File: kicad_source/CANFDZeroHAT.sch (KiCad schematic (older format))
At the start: 24 parts, among them CN1 RASPI-IO, CN2 691322310004, CN3 GH_SM04B-GHS-TB, CN4 GH_SM04B-GHS-TB, SW1 JS202011JCQN, U1 MCP2518FD, U2 TCAN332GDR, Y1 RH100-20.000-20-3030-TR

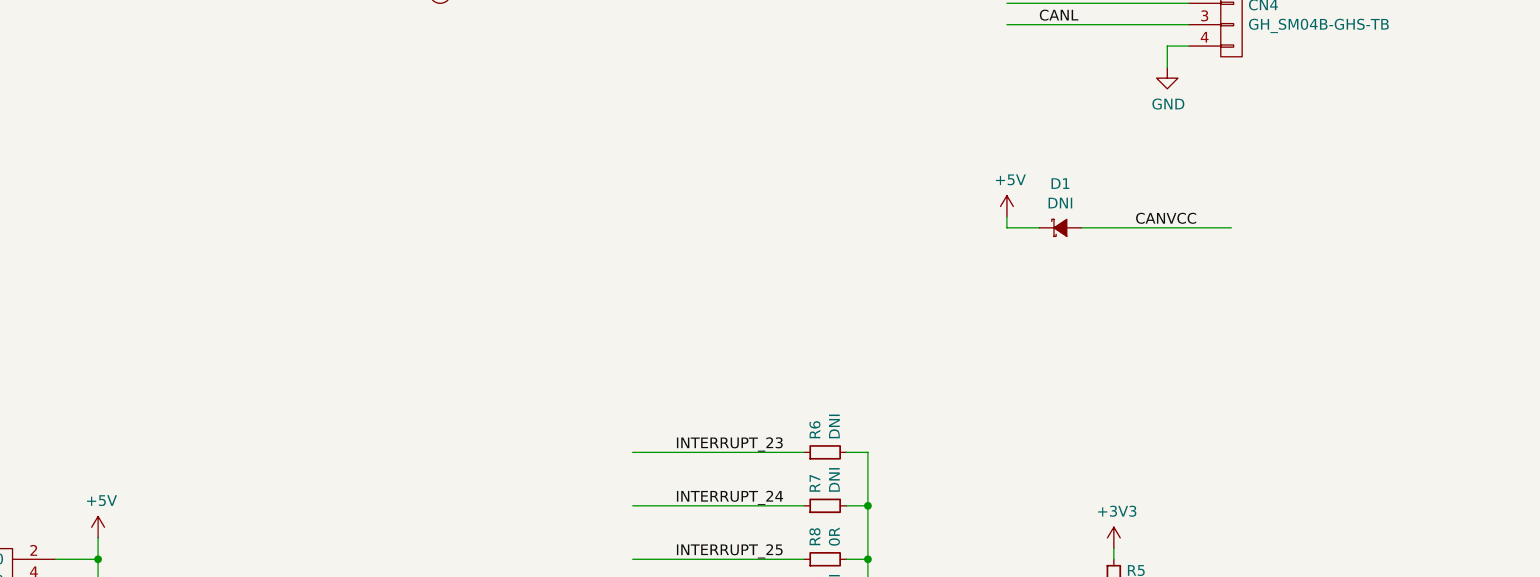
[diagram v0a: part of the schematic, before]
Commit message: updated schematic, added fuse and debug leds
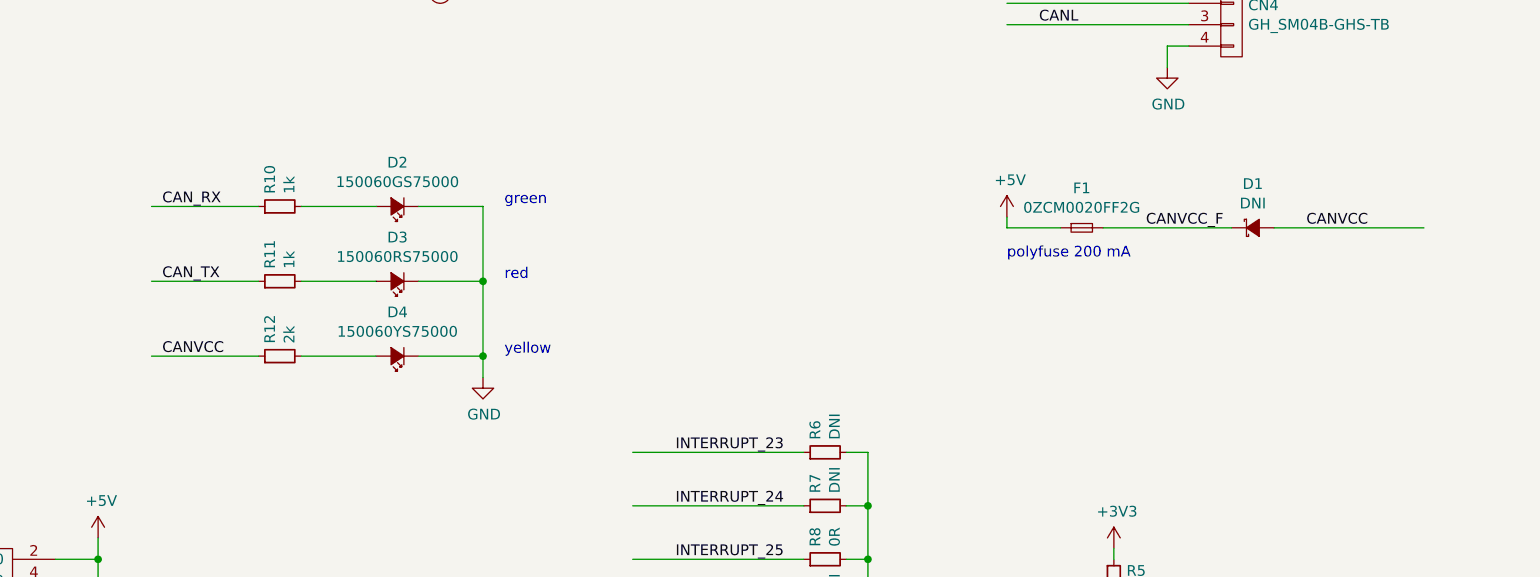
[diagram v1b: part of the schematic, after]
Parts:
- added D2: 150060GS75000, symbol devices:Led_Small
- added D3: 150060RS75000, symbol devices:Led_Small
- added D4: 150060YS75000, symbol devices:Led_Small
- added F1: 0ZCM0020FF2G, resistors:R_0603, symbol devices:F_Small
- added R10, R11: 1k, resistors:R_0603, symbol devices:R_0603
- added R12: 2k, resistors:R_0603, symbol devices:R_0603
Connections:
- net labels added: CANVCC_F
- wire segments 122 -> 135
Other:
- note added: "green"
- note added: "polyfuse 200 mA"
- note added: "red"
- note added: "yellow"
- moved on the sheet: D1
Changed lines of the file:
@@
 Sheet 1 1
 Title "CANFDZeroHAT"
-Date "2020-12-20"
-Rev "0.1"
+Date "2021-01-02"
+Rev "0.2"
 Comp "generationmake"
 Comment1 ""
@@
 L devices:D_Schottky_Small D?
 U 1 1 5FD7527E
-P 9300 3400
+P 10200 3400
 AR Path="/5FD58A5B/5FD7527E" Ref="D?"  Part="1"
 AR Path="/5FD7527E" Ref="D1"  Part="1"
-F 0 "D1" H 9300 3605 50  0000 C CNN
-F 1 "DNI" H 9300 3514 50  0000 C CNN
-F 2 "diodes:SOD-123" V 9300 3400 50  0001 C CNN
-F 3 "" V 9300 3400 50  0000 C CNN
-	1    9300 3400
+F 0 "D1" H 10200 3605 50  0000 C CNN
+F 1 "DNI" H 10200 3514 50  0000 C CNN
+F 2 "diodes:SOD-123" V 10200 3400 50  0001 C CNN
+F 3 "" V 10200 3400 50  0000 C CNN
+	1    10200 3400
 	1    0    0    -1
 $EndComp
@@
 $EndComp
 Wire Wire Line
-	10100 3400 9400 3400
-Wire Wire Line
-	9200 3400 9050 3400
-Wire Wire Line
 	9050 3400 9050 3350
 Text Label 9200 2250 0    50   ~ 0
@@
 Text Label 9200 1300 0    50   ~ 0
 CANVCC
-Text Label 9650 3400 0    50   ~ 0
-CANVCC
+Text Label 9700 3400 0    50   ~ 0
+CANVCC_F
 Wire Wire Line
 	9050 2250 9900 2250
@@
 Wire Wire Line
 	3000 2100 3000 2300
+$Comp
+L devices:F_Small F1
+U 1 1 5FF07EC2
+P 9400 3400
+F 0 "F1" H 9400 3585 50  0000 C CNN
+F 1 "0ZCM0020FF2G" H 9400 3494 50  0000 C CNN
+F 2 "resistors:R_0603" H 9400 3400 50  0001 C CNN
+F 3 "" H 9400 3400 50  0000 C CNN
+	1    9400 3400
+	1    0    0    -1
+$EndComp
+Text Label 10450 3400 0    50   ~ 0
+CANVCC
+Text Notes 9050 3550 0    50   ~ 0
+polyfuse 200 mA
+Wire Wire Line
+	9050 3400 9300 3400
+Wire Wire Line
+	9500 3400 10100 3400
+Wire Wire Line
+	11000 3400 10300 3400
+$Comp
+L devices:Led_Small D2
+U 1 1 5FF1A54D
+P 6200 3300
+F 0 "D2" H 6200 3095 50  0000 C CNN
+F 1 "150060GS75000" H 6200 3186 50  0000 C CNN
+F 2 "" V 6200 3300 50  0000 C CNN
+F 3 "" V 6200 3300 50  0000 C CNN
+	1    6200 3300
+	-1   0    0    1
+$EndComp
+$Comp
+L devices:R_0603 R?
+U 1 1 5FF1C600
+P 5650 3300
+AR Path="/5FD58A5B/5FF1C600" Ref="R?"  Part="1"
+AR Path="/5FF1C600" Ref="R10"  Part="1"
+F 0 "R10" H 5709 3346 50  0000 L CNN
+F 1 "1k" H 5709 3255 50  0000 L CNN
+F 2 "resistors:R_0603" H 5650 3150 50  0001 C CNN
+F 3 "" H 5650 3300 50  0000 C CNN
+	1    5650 3300
+	0    -1   -1   0
+$EndComp
+Text Notes 6700 3300 0    50   ~ 0
+green
+$Comp
+L devices:Led_Small D3
+U 1 1 5FF1E649
+P 6200 3650
+F 0 "D3" H 6200 3445 50  0000 C CNN
+F 1 "150060RS75000" H 6200 3536 50  0000 C CNN
+F 2 "" V 6200 3650 50  0000 C CNN
+F 3 "" V 6200 3650 50  0000 C CNN
+	1    6200 3650
+	-1   0    0    1
+$EndComp
+$Comp
+L devices:R_0603 R?
+U 1 1 5FF1E7A3
+P 5650 3650
+AR Path="/5FD58A5B/5FF1E7A3" Ref="R?"  Part="1"
+AR Path="/5FF1E7A3" Ref="R11"  Part="1"
+F 0 "R11" H 5709 3696 50  0000 L CNN
+F 1 "1k" H 5709 3605 50  0000 L CNN
+F 2 "resistors:R_0603" H 5650 3500 50  0001 C CNN
+F 3 "" H 5650 3650 50  0000 C CNN
+	1    5650 3650
+	0    -1   -1   0
+$EndComp
+Text Notes 6700 3650 0    50   ~ 0
+red
+$Comp
+L devices:Led_Small D4
+U 1 1 5FF239FB
+P 6200 4000
+F 0 "D4" H 6200 3795 50  0000 C CNN
+F 1 "150060YS75000" H 6200 3886 50  0000 C CNN
+F 2 "" V 6200 4000 50  0000 C CNN
+F 3 "" V 6200 4000 50  0000 C CNN
+	1    6200 4000
+	-1   0    0    1
+$EndComp
+$Comp
+L devices:R_0603 R?
+U 1 1 5FF23B7B
+P 5650 4000
+AR Path="/5FD58A5B/5FF23B7B" Ref="R?"  Part="1"
+AR Path="/5FF23B7B" Ref="R12"  Part="1"
+F 0 "R12" H 5709 4046 50  0000 L CNN
+F 1 "2k" H 5709 3955 50  0000 L CNN
+F 2 "resistors:R_0603" H 5650 3850 50  0001 C CNN
+F 3 "" H 5650 4000 50  0000 C CNN
+	1    5650 4000
+	0    -1   -1   0
+$EndComp
+Text Notes 6700 4000 0    50   ~ 0
+yellow
+$Comp
+L power-supply:GND #PWR?
+U 1 1 5FF295E3
+P 6600 4100
+AR Path="/5FD58A5B/5FF295E3" Ref="#PWR?"  Part="1"
+AR Path="/5FF295E3" Ref="#PWR017"  Part="1"
+F 0 "#PWR017" H 6600 3850 50  0001 C CNN
+F 1 "GND" H 6605 3927 50  0000 C CNN
+F 2 "" H 6600 4100 50  0000 C CNN
+F 3 "" H 6600 4100 50  0000 C CNN
+	1    6600 4100
+	1    0    0    -1
+$EndComp
+Wire Wire Line
+	6300 3300 6600 3300
+Wire Wire Line
+	6600 3300 6600 3650
+Wire Wire Line
+	5050 3300 5550 3300
+Wire Wire Line
+	5050 3650 5550 3650
+Wire Wire Line
+	5050 4000 5550 4000
+Wire Wire Line
+	5750 3300 6100 3300
+Wire Wire Line
+	5750 3650 6100 3650
+Wire Wire Line
+	5750 4000 6100 4000
+Wire Wire Line
+	6300 3650 6600 3650
+Connection ~ 6600 3650
+Wire Wire Line
+	6600 3650 6600 4000
+Wire Wire Line
+	6300 4000 6600 4000
+Connection ~ 6600 4000
+Wire Wire Line
+	6600 4000 6600 4100
+Text Label 5100 3650 0    50   ~ 0
+CAN_TX
+Text Label 5100 3300 0    50   ~ 0
+CAN_RX
+Text Label 5100 4000 0    50   ~ 0
+CANVCC
 $EndSCHEMATC
